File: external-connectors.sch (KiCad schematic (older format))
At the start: 3 parts

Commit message: created 8284A clock generator block
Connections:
- net RESET: now reaches J?.7 (Pin_7)
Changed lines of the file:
@@
 $Descr A4 11693 8268
 encoding utf-8
-Sheet 3 3
+Sheet 3 4
 Title "external-connectors"
 Date ""
@@
 Wire Wire Line
 	8200 3600 7500 3600
-Text HLabel 4100 4750 0    50   Input ~ 0
+Text HLabel 4100 4750 0    50   Output ~ 0
 CLK
-Text HLabel 4600 4750 2    50   Input ~ 0
-~BHE
-Wire Bus Line
-	6050 1950 8550 1950
-Wire Bus Line
-	1900 1950 4650 1950
-Text HLabel 4100 4850 0    50   Input ~ 0
+Text HLabel 4100 4850 0    50   UnSpc ~ 0
 ~MRDC
 Text HLabel 4100 4950 0    50   Input ~ 0
 ~MWTC
-Text HLabel 4600 4850 2    50   Input ~ 0
+Text HLabel 4600 4850 2    50   Output ~ 0
 ~IORC
-Text HLabel 4600 4950 2    50   Input ~ 0
+Text HLabel 4600 4950 2    50   Output ~ 0
 ~IOWC
 $Comp
@@
 	1    0    0    -1
 $EndComp
+Wire Bus Line
+	6050 1950 8550 1950
+Wire Bus Line
+	1900 1950 4650 1950
+Text HLabel 4100 5050 0    50   Input ~ 0
+RESET
+Text HLabel 4600 4750 2    50   Output ~ 0
+~BHE
 $EndSCHEMATC

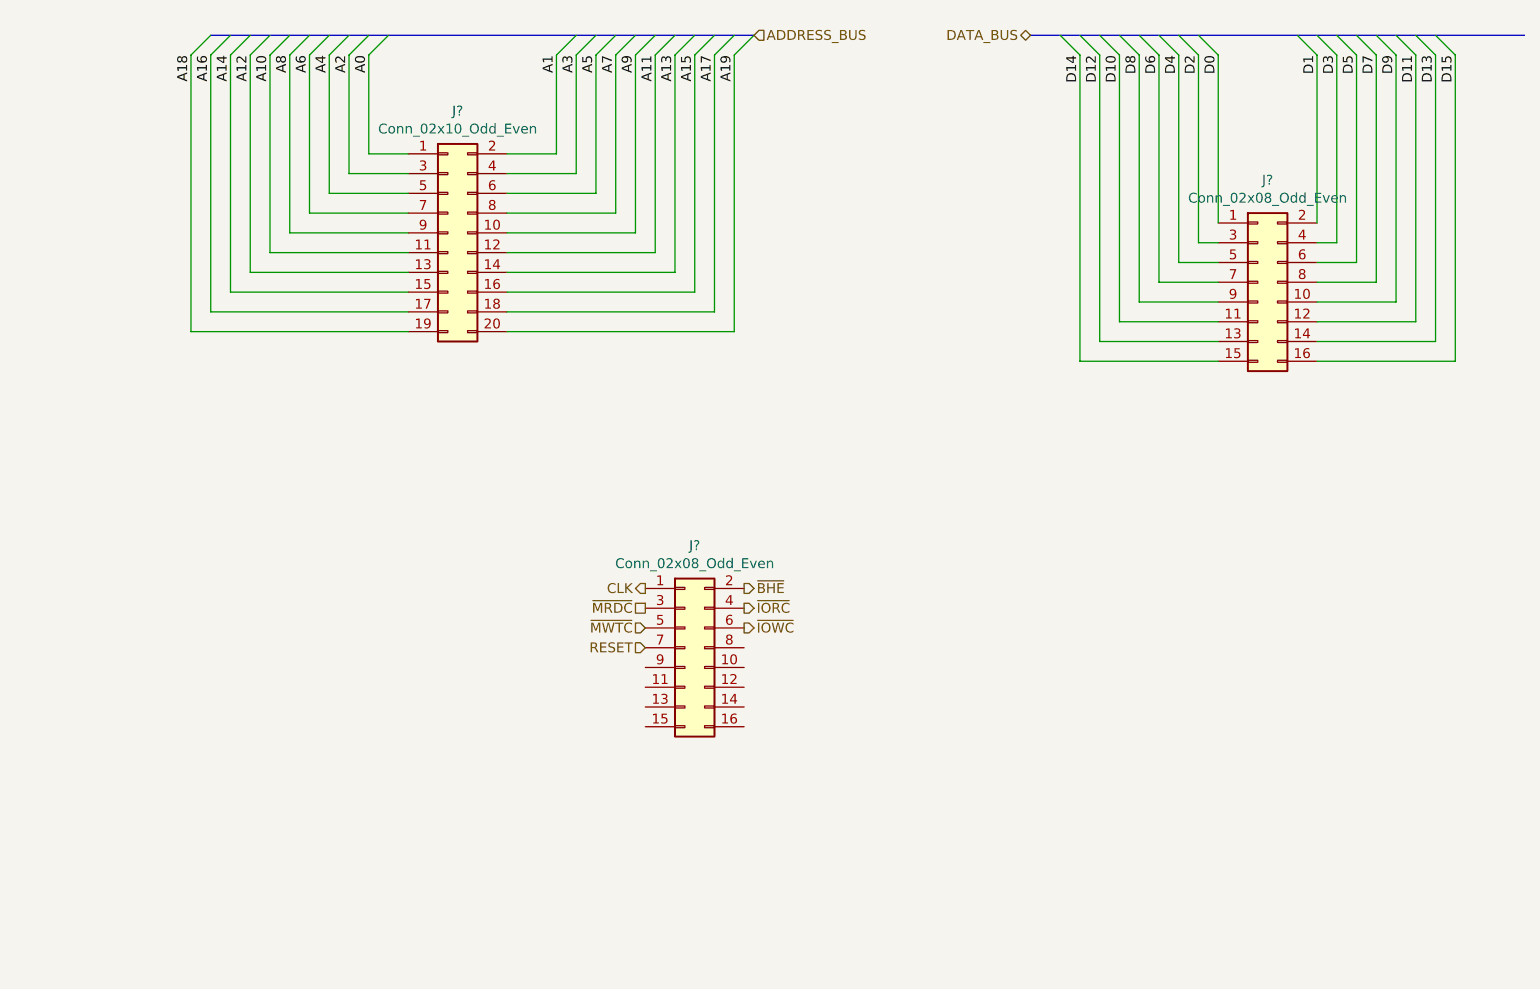
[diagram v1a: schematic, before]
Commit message: created 28F010 CMOS flash block; improved power decoupling; added M/~IO pin from 8086 sheet; reduced no. of logic gates in 8086 processor block; added +12V; moved input power to external-connectors sheet; annotated schematics
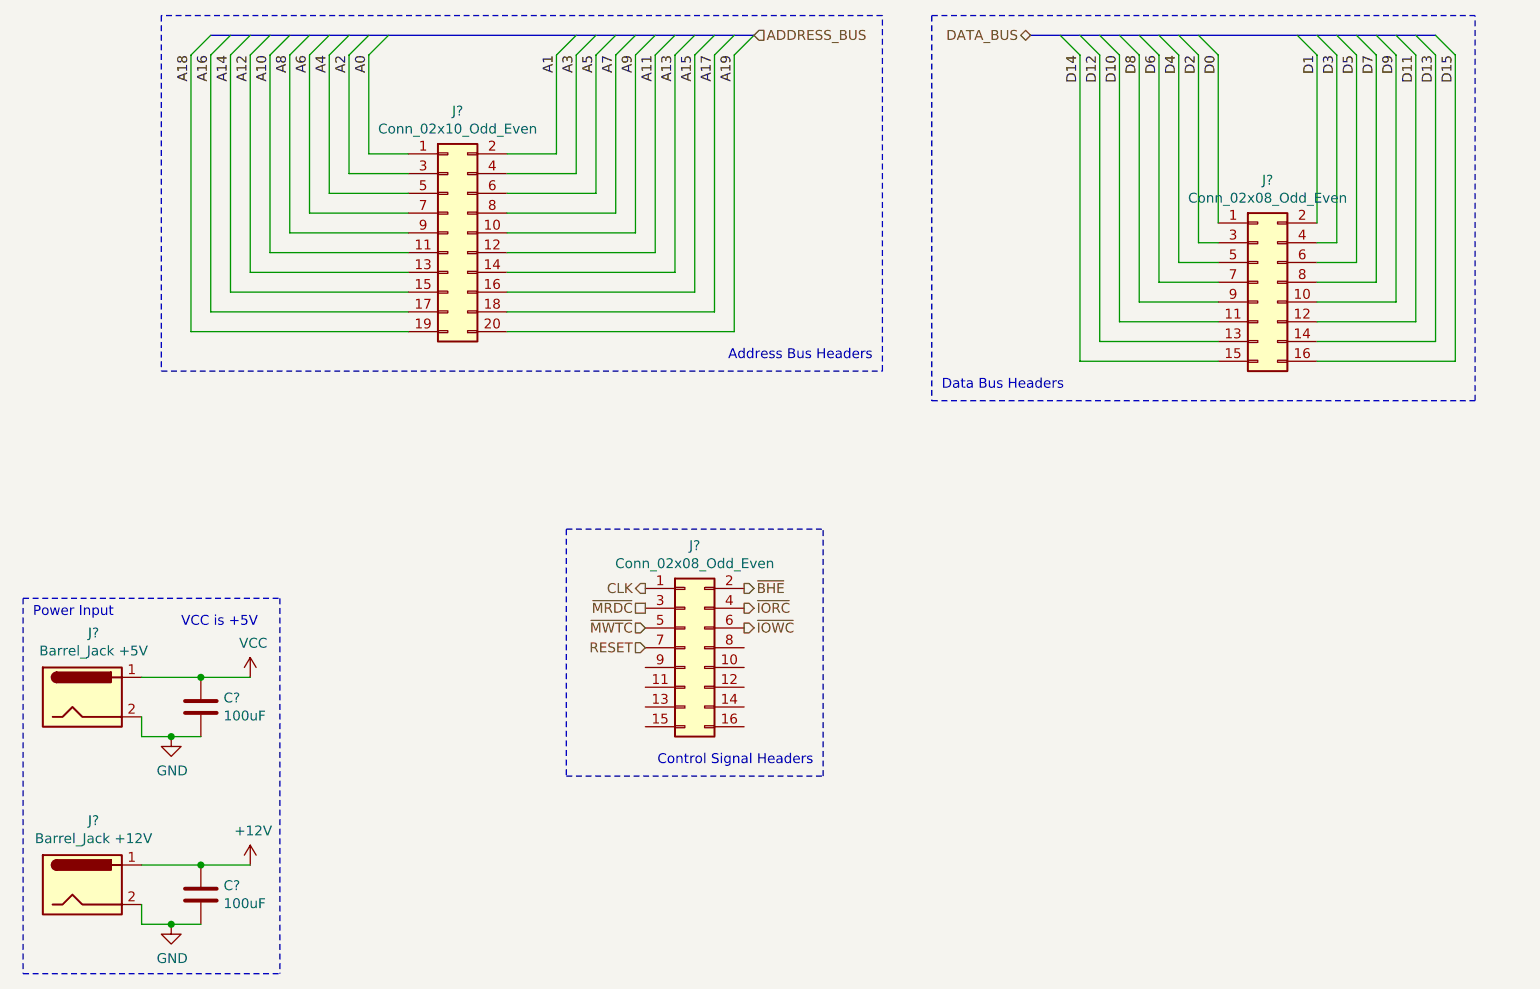
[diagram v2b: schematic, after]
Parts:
- added C? (x2): 100uF, symbol Device:C
- added J?: Barrel_Jack +5V, symbol Connector:Barrel_Jack
- added J?: Barrel_Jack +12V, symbol Connector:Barrel_Jack
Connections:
- new net +12V: C?.1, J?.1
- new net GND: C?.2, C?.2, J?.2, J?.2
- new net VCC: C?.1, J?.1
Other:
- note added: "Address Bus Headers"
- note added: "Control Signal Headers"
- note added: "Data Bus Headers"
- note added: "Power Input"
- note added: "VCC is +5V"
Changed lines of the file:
@@
 $Descr A4 11693 8268
 encoding utf-8
-Sheet 3 4
+Sheet 3 5
 Title "external-connectors"
 Date ""
@@
 	1    0    0    -1
 $EndComp
-Wire Bus Line
-	6050 1950 8550 1950
-Wire Bus Line
-	1900 1950 4650 1950
 Text HLabel 4100 5050 0    50   Input ~ 0
 RESET
 Text HLabel 4600 4750 2    50   Output ~ 0
 ~BHE
+$Comp
+L power:GND #PWR?
+U 1 1 61D25BC8
+P 1700 5500
+F 0 "#PWR?" H 1700 5250 50  0001 C CNN
+F 1 "GND" H 1705 5327 50  0000 C CNN
+F 2 "" H 1700 5500 50  0001 C CNN
+F 3 "" H 1700 5500 50  0001 C CNN
+	1    1700 5500
+	1    0    0    -1
+$EndComp
+$Comp
+L power:VCC #PWR?
+U 1 1 61D25BCE
+P 2100 5200
+F 0 "#PWR?" H 2100 5050 50  0001 C CNN
+F 1 "VCC" H 2115 5373 50  0000 C CNN
+F 2 "" H 2100 5200 50  0001 C CNN
+F 3 "" H 2100 5200 50  0001 C CNN
+	1    2100 5200
+	1    0    0    -1
+$EndComp
+$Comp
+L Device:C C?
+U 1 1 61D25BD4
+P 1850 5350
+F 0 "C?" H 1965 5396 50  0000 L CNN
+F 1 "100uF" H 1965 5305 50  0000 L CNN
+F 2 "" H 1888 5200 50  0001 C CNN
+F 3 "~" H 1850 5350 50  0001 C CNN
+	1    1850 5350
+	1    0    0    -1
+$EndComp
+Wire Wire Line
+	1550 5200 1850 5200
+Wire Wire Line
+	2100 5200 1850 5200
+Connection ~ 1850 5200
+Wire Wire Line
+	1850 5500 1700 5500
+Wire Wire Line
+	1550 5400 1550 5500
+Wire Wire Line
+	1550 5500 1700 5500
+Connection ~ 1700 5500
+$Comp
+L Connector:Barrel_Jack J?
+U 1 1 61D2B6EC
+P 1250 6250
+AR Path="/61D2B6EC" Ref="J?"  Part="1"
+AR Path="/626E3AF4/61D2B6EC" Ref="J?"  Part="1"
+F 0 "J?" H 1307 6575 50  0000 C CNN
+F 1 "Barrel_Jack +12V" H 1307 6484 50  0000 C CNN
+F 2 "" H 1300 6210 50  0001 C CNN
+F 3 "~" H 1300 6210 50  0001 C CNN
+	1    1250 6250
+	1    0    0    -1
+$EndComp
+$Comp
+L power:GND #PWR?
+U 1 1 61D2B6F2
+P 1700 6450
+F 0 "#PWR?" H 1700 6200 50  0001 C CNN
+F 1 "GND" H 1705 6277 50  0000 C CNN
+F 2 "" H 1700 6450 50  0001 C CNN
+F 3 "" H 1700 6450 50  0001 C CNN
+	1    1700 6450
+	1    0    0    -1
+$EndComp
+$Comp
+L Device:C C?
+U 1 1 61D2B6FE
+P 1850 6300
+F 0 "C?" H 1965 6346 50  0000 L CNN
+F 1 "100uF" H 1965 6255 50  0000 L CNN
+F 2 "" H 1888 6150 50  0001 C CNN
+F 3 "~" H 1850 6300 50  0001 C CNN
+	1    1850 6300
+	1    0    0    -1
+$EndComp
+Wire Wire Line
+	1550 6150 1850 6150
+Wire Wire Line
+	2100 6150 1850 6150
+Connection ~ 1850 6150
+Wire Wire Line
+	1850 6450 1700 6450
+Wire Wire Line
+	1550 6350 1550 6450
+Wire Wire Line
+	1550 6450 1700 6450
+Connection ~ 1700 6450
+$Comp
+L power:+12V #PWR?
+U 1 1 61D30CC5
+P 2100 6150
+F 0 "#PWR?" H 2100 6000 50  0001 C CNN
+F 1 "+12V" H 2115 6323 50  0000 C CNN
+F 2 "" H 2100 6150 50  0001 C CNN
+F 3 "" H 2100 6150 50  0001 C CNN
+	1    2100 6150
+	1    0    0    -1
+$EndComp
+Wire Notes Line
+	2250 4800 2250 6700
+Wire Notes Line
+	950  4800 950  6700
+Wire Notes Line
+	5300 1850 1650 1850
+Wire Notes Line
+	1650 3650 5300 3650
+Wire Notes Line
+	5550 3800 8300 3800
+Wire Notes Line
+	8300 3800 8300 1850
+Wire Notes Line
+	5550 1850 8300 1850
+Wire Notes Line
+	5550 1850 5550 3800
+Text Notes 5600 3750 0    50   ~ 0
+Data Bus Headers
+Wire Notes Line
+	5300 3650 5300 1850
+Wire Notes Line
+	1650 1850 1650 3650
+Text Notes 5250 3600 2    50   ~ 0
+Address Bus Headers
+Text Notes 1000 4900 0    50   ~ 0
+Power Input
+Text Notes 1750 4950 0    50   ~ 0
+VCC is +5V
+$Comp
+L Connector:Barrel_Jack J?
+U 1 1 61D25BC2
+P 1250 5300
+AR Path="/61D25BC2" Ref="J?"  Part="1"
+AR Path="/626E3AF4/61D25BC2" Ref="J?"  Part="1"
+F 0 "J?" H 1307 5625 50  0000 C CNN
+F 1 "Barrel_Jack +5V" H 1307 5534 50  0000 C CNN
+F 2 "" H 1300 5260 50  0001 C CNN
+F 3 "~" H 1300 5260 50  0001 C CNN
+	1    1250 5300
+	1    0    0    -1
+$EndComp
+Wire Notes Line
+	950  6700 2250 6700
+Wire Notes Line
+	950  4800 2250 4800
+Wire Notes Line
+	3700 4450 3700 5700
+Wire Notes Line
+	3700 5700 5000 5700
+Wire Notes Line
+	5000 5700 5000 4450
+Wire Notes Line
+	3700 4450 5000 4450
+Wire Bus Line
+	6050 1950 8100 1950
+Wire Bus Line
+	1900 1950 4650 1950
+Text Notes 4950 5650 2    50   ~ 0
+Control Signal Headers
 $EndSCHEMATC
